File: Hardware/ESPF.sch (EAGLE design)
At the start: 24 parts, among them IC1 CP2102N-A01-GQFN24, J2 USB-C-16P-16P, J3 ESP-PROG-1X6-2.54-PINS-RA, Q1 MMDT3904

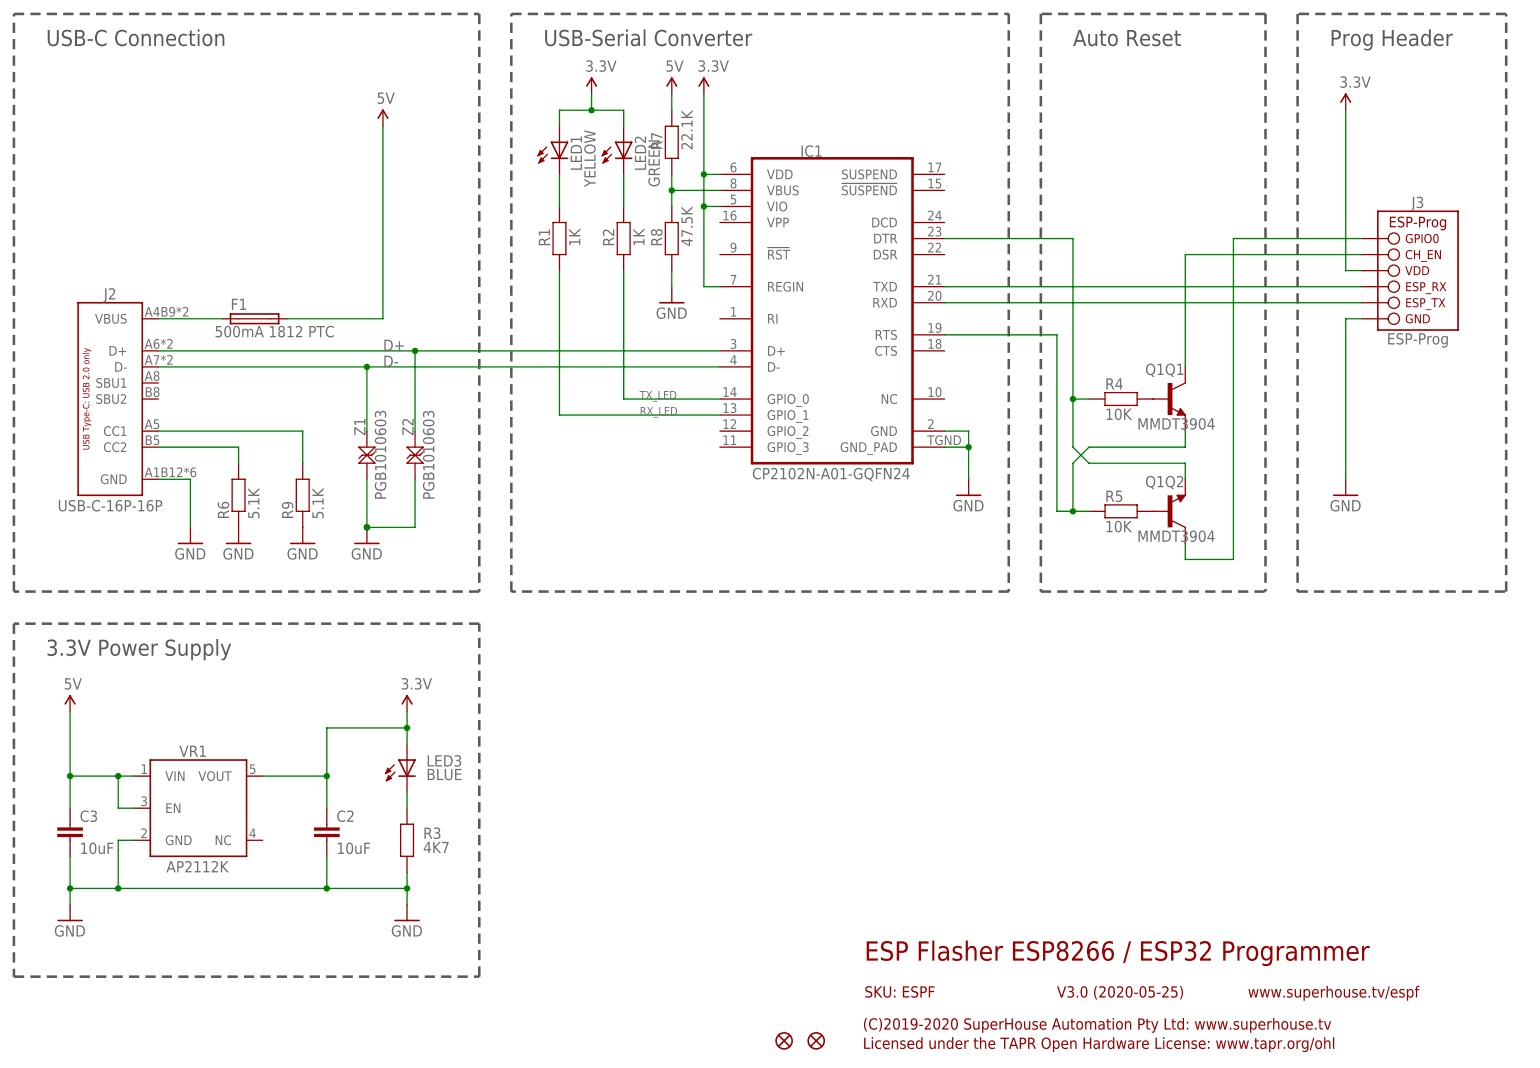
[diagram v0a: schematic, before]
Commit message: Replace ESPFlash header using part from dedicated library.
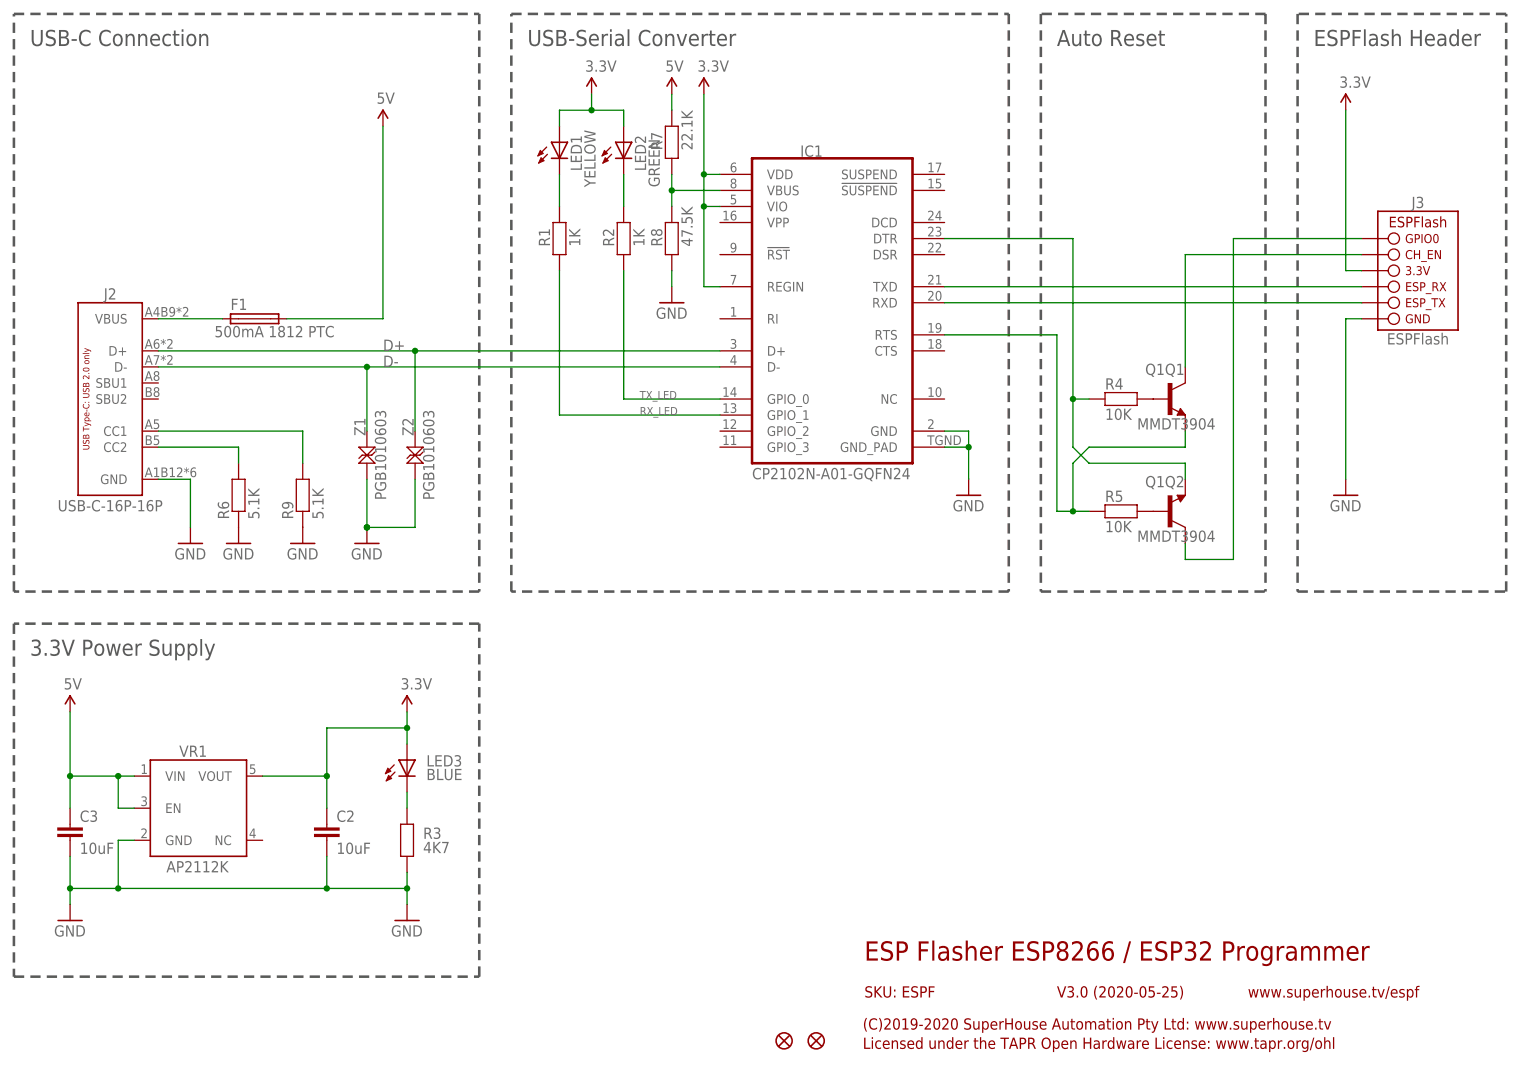
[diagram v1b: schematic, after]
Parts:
- FID1, FID2: device freetronics:FIDUCIAL1X2.5 -> SuperHouse-Symbols:FIDUCIAL1X2.5
- J3: value ESP-PROG-1X6-2.54-PINS-RA -> ESPFLASH-1X6-2.54-PINS-RA; device SuperHouse-ESP-Prog:ESP-PROG-1X6-2.54-PINS-RA -> SuperHouse-ESPFlash:ESPFLASH-1X6-2.54-PINS-RA
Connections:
- net 3.3V: now also J3.3.3V; no longer J3.VDD
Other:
- note added: "ESPFlash Header"
- note removed: "Prog Header"
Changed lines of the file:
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@@
 <?xml version="1.0" encoding="utf-8"?>
 <!DOCTYPE eagle SYSTEM "eagle.dtd">
-<eagle version="9.6.1">
+<eagle version="9.6.2">
 <drawing>
 <settings>
@@
 <part name="GND2" library="SuperHouse-SupplySymbols" library_urn="urn:adsk.eagle:library:11790503" deviceset="GND" device=""/>
 <part name="GND8" library="SuperHouse-SupplySymbols" library_urn="urn:adsk.eagle:library:11790503" deviceset="GND" device=""/>
-<part name="FID1" library="freetronics" deviceset="FIDUCIAL" device="1X2.5"/>
-<part name="FID2" library="freetronics" deviceset="FIDUCIAL" device="1X2.5"/>
-<part name="J3" library="SuperHouse-ESP-Prog" library_urn="urn:adsk.eagle:library:14353672" deviceset="ESP-PROG" device="-1X6-2.54-PINS-RA" package3d_urn="urn:adsk.eagle:package:20465662/6"/>
+<part name="FID1" library="SuperHouse-Symbols" library_urn="urn:adsk.eagle:library:13228893" deviceset="FIDUCIAL" device="1X2.5" package3d_urn="urn:adsk.eagle:package:13228898/2"/>
+<part name="FID2" library="SuperHouse-Symbols" library_urn="urn:adsk.eagle:library:13228893" deviceset="FIDUCIAL" device="1X2.5" package3d_urn="urn:adsk.eagle:package:13228898/2"/>
+<part name="J3" library="SuperHouse-ESPFlash" library_urn="urn:adsk.eagle:library:23117902" deviceset="ESPFLASH" device="-1X6-2.54-PINS-RA" package3d_urn="urn:adsk.eagle:package:20465662/7"/>
 <part name="P+1" library="SuperHouse-SupplySymbols" library_urn="urn:adsk.eagle:library:11790503" deviceset="3.3V" device=""/>
 <part name="GND9" library="SuperHouse-SupplySymbols" library_urn="urn:adsk.eagle:library:11790503" deviceset="GND" device=""/>
@@
 <wire x1="243.84" y1="78.74" x2="243.84" y2="170.18" width="0.4064" layer="97" style="longdash"/>
 <wire x1="243.84" y1="170.18" x2="210.82" y2="170.18" width="0.4064" layer="97" style="longdash"/>
-<text x="12.7" y="165.1" size="2.54" layer="97">USB-C Connection</text>
-<text x="91.44" y="165.1" size="2.54" layer="97">USB-Serial Converter</text>
-<text x="175.26" y="165.1" size="2.54" layer="97">Auto Reset</text>
-<text x="215.9" y="165.1" size="2.54" layer="97">Prog Header</text>
-<text x="12.7" y="68.58" size="2.54" layer="97">3.3V Power Supply</text>
+<text x="10.16" y="165.1" size="2.54" layer="97">USB-C Connection</text>
+<text x="88.9" y="165.1" size="2.54" layer="97">USB-Serial Converter</text>
+<text x="172.72" y="165.1" size="2.54" layer="97">Auto Reset</text>
+<text x="213.36" y="165.1" size="2.54" layer="97">ESPFlash Header</text>
+<text x="10.16" y="68.58" size="2.54" layer="97">3.3V Power Supply</text>
 <wire x1="7.62" y1="73.66" x2="7.62" y2="17.78" width="0.4064" layer="97" style="longdash"/>
 <wire x1="7.62" y1="17.78" x2="81.28" y2="17.78" width="0.4064" layer="97" style="longdash"/>
@@
 </segment>
 <segment>
-<pinref part="J3" gate="G$1" pin="VDD"/>
+<pinref part="J3" gate="G$1" pin="3.3V"/>
 <wire x1="220.98" y1="129.54" x2="218.44" y2="129.54" width="0.1524" layer="91"/>
 <pinref part="P+1" gate="G$1" pin="3.3V"/>

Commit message: Added 100nF cap on reset line of target device. Added tab to support right angle header. Added note about ESPFlash convention in schematic.
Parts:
- removed J3: ESPFLASH-1X6-2.54-PINS-RA, SuperHouse-ESPFlash:ESPFLASH-1X6-2.54-PINS-RA
- added C1: 10uF, SuperHouse-DiscreteSemi:CAP0603
- added J1: USB-C-16P-16P, SuperHouse-Connectors:USB-C-16P-16P
- C2: device SuperHouse-DiscreteSemi:CAP0805 -> SuperHouse-DiscreteSemi:CAP0603
- C3: value 10uF -> 100nF; device SuperHouse-DiscreteSemi:CAP0805 -> SuperHouse-DiscreteSemi:CAP0603
- J2: value USB-C-16P-16P -> ESPFLASH-1X6-2.54-PINS-RA; device SuperHouse-Connectors:USB-C-16P-16P -> SuperHouse-ESPFlash:ESPFLASH-1X6-2.54-PINS-RA
- VR1: value AP2112KSOT25 -> AP2112K-3.3
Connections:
- net 3.3V: now also J2.3.3V; no longer J3.3.3V
- net 5V: now also C1.1; no longer C3.1
- net D+: now also J1.D+; no longer J2.D+
- net D-: now also J1.D-; no longer J2.D-
- net EN: now also C3.1, J2.CH_EN; no longer J3.CH_EN
- net GND: now also C1.2, J1.GND; no longer J3.GND
- net GPIO0: now also J2.GPIO0; no longer J3.GPIO0
- net N$10: now also J1.CC1; no longer J2.CC1
- net N$9: now also J1.CC2; no longer J2.CC2
- net RXI: now also J2.ESP_TX; no longer J3.ESP_TX
- net TXO: now also J2.ESP_RX; no longer J3.ESP_RX
- net VIN: now also J1.VBUS; no longer J2.VBUS
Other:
- note added: "(C)2019-2021 SuperHouse Automation Pty Ltd: www.superhouse.tv"
- note added: "1"
- note added: "2"
- note added: "3"
- note added: "4"
- note added: "5"
- note added: "6"
- note added: "For more information about the ESPFlash programming header convention, please see www.superhouse.tv/espflash"
- note added: "V3.2 (2021-05-06)"
- note removed: "(C)2019-2020 SuperHouse Automation Pty Ltd: www.superhouse.tv"
- note removed: "V3.0 (2020-05-25)"
- moved on the sheet: C3, F1, IC1, LED1, LED2, Q1Q1, Q1Q2, R1, R2, R4, R5, R6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
